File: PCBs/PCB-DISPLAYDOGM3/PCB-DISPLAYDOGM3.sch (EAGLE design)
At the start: 20 parts, among them IC2 74HC14D

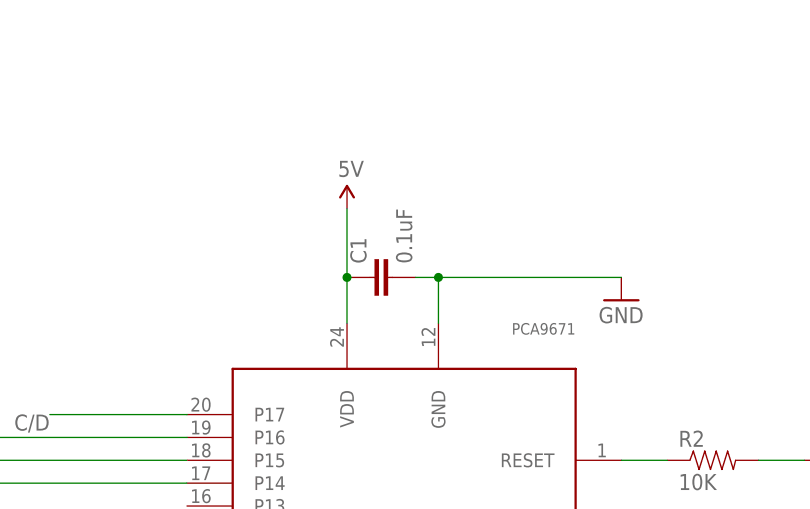
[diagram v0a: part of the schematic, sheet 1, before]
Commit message: Added SKAARHOJ_ID to a lot of PCBs...
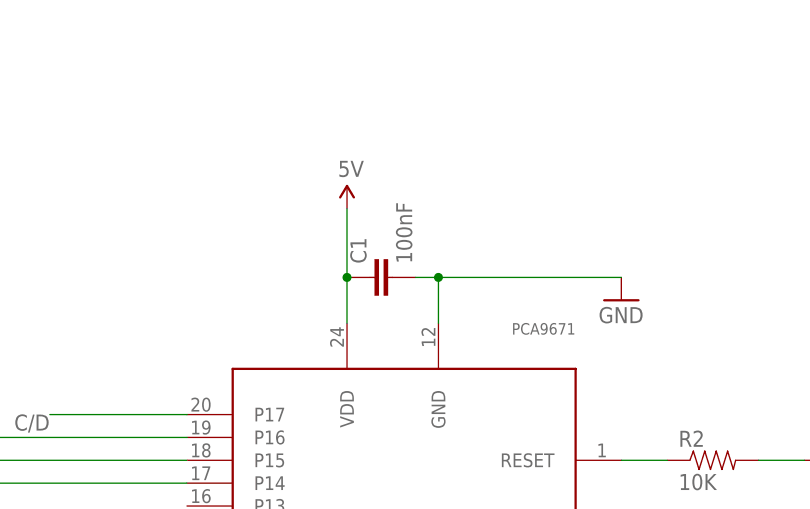
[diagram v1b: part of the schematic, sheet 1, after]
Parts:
- C1: value 0.1uF -> 100nF
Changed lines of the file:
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@@
 <?xml version="1.0" encoding="utf-8"?>
 <!DOCTYPE eagle SYSTEM "eagle.dtd">
-<eagle version="7.5.0">
+<eagle version="7.7.0">
 <drawing>
 <settings>
@@
 <grid distance="0.1" unitdist="inch" unit="inch" style="lines" multiple="1" display="no" altdistance="0.01" altunitdist="inch" altunit="inch"/>
 <layers>
-<layer number="1" name="Top" color="4" fill="1" visible="yes" active="no"/>
-<layer number="2" name="Route2" color="1" fill="3" visible="yes" active="no"/>
-<layer number="3" name="Route3" color="4" fill="3" visible="yes" active="no"/>
-<layer number="4" name="Route4" color="1" fill="4" visible="yes" active="no"/>
-<layer number="5" name="Route5" color="4" fill="4" visible="yes" active="no"/>
-<layer number="6" name="Route6" color="1" fill="8" visible="yes" active="no"/>
-<layer number="7" name="Route7" color="4" fill="8" visible="yes" active="no"/>
-<layer number="8" name="Route8" color="1" fill="2" visible="yes" active="no"/>
-<layer number="9" name="Route9" color="4" fill="2" visible="yes" active="no"/>
-<layer number="10" name="Route10" color="1" fill="7" visible="yes" active="no"/>
-<layer number="11" name="Route11" color="4" fill="7" visible="yes" active="no"/>
-<layer number="12" name="Route12" color="1" fill="5" visible="yes" active="no"/>
-<layer number="13" name="Route13" color="4" fill="5" visible="yes" active="no"/>
-<layer number="14" name="Route14" color="1" fill="6" visible="yes" active="no"/>
-<layer number="15" name="Route15" color="4" fill="6" visible="yes" active="no"/>
-<layer number="16" name="Bottom" color="1" fill="1" visible="yes" active="no"/>
-<layer number="17" name="Pads" color="2" fill="1" visible="yes" active="no"/>
-<layer number="18" name="Vias" color="2" fill="1" visible="yes" active="no"/>
-<layer number="19" name="Unrouted" color="13" fill="1" visible="yes" active="no"/>
-<layer number="20" name="Dimension" color="15" fill="1" visible="yes" active="no"/>
-<layer number="21" name="tPlace" color="7" fill="1" visible="yes" active="no"/>
-<layer number="22" name="bPlace" color="7" fill="1" visible="yes" active="no"/>
-<layer number="23" name="tOrigins" color="15" fill="1" visible="yes" active="no"/>
-<layer number="24" name="bOrigins" color="15" fill="1" visible="yes" active="no"/>
-<layer number="25" name="tNames" color="7" fill="1" visible="yes" active="no"/>
-<layer number="26" name="bNames" color="7" fill="1" visible="yes" active="no"/>
-<layer number="27" name="tValues" color="7" fill="1" visible="yes" active="no"/>
-<layer number="28" name="bValues" color="7" fill="1" visible="yes" active="no"/>
+<layer number="1" name="Top" color="4" fill="1" visible="no" active="no"/>
+<layer number="2" name="Route2" color="1" fill="3" visible="no" active="no"/>
+<layer number="3" name="Route3" color="4" fill="3" visible="no" active="no"/>
+<layer number="4" name="Route4" color="1" fill="4" visible="no" active="no"/>
+<layer number="5" name="Route5" color="4" fill="4" visible="no" active="no"/>
+<layer number="6" name="Route6" color="1" fill="8" visible="no" active="no"/>
+<layer number="7" name="Route7" color="4" fill="8" visible="no" active="no"/>
+<layer number="8" name="Route8" color="1" fill="2" visible="no" active="no"/>
+<layer number="9" name="Route9" color="4" fill="2" visible="no" active="no"/>
+<layer number="10" name="Route10" color="1" fill="7" visible="no" active="no"/>
+<layer number="11" name="Route11" color="4" fill="7" visible="no" active="no"/>
+<layer number="12" name="Route12" color="1" fill="5" visible="no" active="no"/>
+<layer number="13" name="Route13" color="4" fill="5" visible="no" active="no"/>
+<layer number="14" name="Route14" color="1" fill="6" visible="no" active="no"/>
+<layer number="15" name="Route15" color="4" fill="6" visible="no" active="no"/>
+<layer number="16" name="Bottom" color="1" fill="1" visible="no" active="no"/>
+<layer number="17" name="Pads" color="2" fill="1" visible="no" active="no"/>
+<layer number="18" name="Vias" color="2" fill="1" visible="no" active="no"/>
+<layer number="19" name="Unrouted" color="13" fill="1" visible="no" active="no"/>
+<layer number="20" name="Dimension" color="15" fill="1" visible="no" active="no"/>
+<layer number="21" name="tPlace" color="7" fill="1" visible="no" active="no"/>
+<layer number="22" name="bPlace" color="7" fill="1" visible="no" active="no"/>
+<layer number="23" name="tOrigins" color="15" fill="1" visible="no" active="no"/>
+<layer number="24" name="bOrigins" color="15" fill="1" visible="no" active="no"/>
+<layer number="25" name="tNames" color="7" fill="1" visible="no" active="no"/>
+<layer number="26" name="bNames" color="7" fill="1" visible="no" active="no"/>
+<layer number="27" name="tValues" color="7" fill="1" visible="no" active="no"/>
+<layer number="28" name="bValues" color="7" fill="1" visible="no" active="no"/>
 <layer number="29" name="tStop" color="7" fill="3" visible="no" active="no"/>
 <layer number="30" name="bStop" color="7" fill="6" visible="no" active="no"/>
@@
 <layer number="35" name="tGlue" color="7" fill="4" visible="no" active="no"/>
 <layer number="36" name="bGlue" color="7" fill="5" visible="no" active="no"/>
-<layer number="37" name="tTest" color="7" fill="1" visible="yes" active="no"/>
-<layer number="38" name="bTest" color="7" fill="1" visible="yes" active="no"/>
+<layer number="37" name="tTest" color="7" fill="1" visible="no" active="no"/>
+<layer number="38" name="bTest" color="7" fill="1" visible="no" active="no"/>
 <layer number="39" name="tKeepout" color="4" fill="11" visible="no" active="no"/>
 <layer number="40" name="bKeepout" color="1" fill="11" visible="no" active="no"/>
@@
 <layer number="44" name="Drills" color="7" fill="1" visible="no" active="no"/>
 <layer number="45" name="Holes" color="7" fill="1" visible="no" active="no"/>
-<layer number="46" name="Milling" color="3" fill="1" visible="yes" active="no"/>
-<layer number="47" name="Measures" color="7" fill="1" visible="yes" active="no"/>
-<layer number="48" name="Document" color="7" fill="1" visible="yes" active="no"/>
-<layer number="49" name="Reference" color="7" fill="1" visible="yes" active="no"/>
-<layer number="50" name="dxf" color="7" fill="1" visible="yes" active="no"/>
-<layer number="51" name="tDocu" color="7" fill="1" visible="yes" active="no"/>
-<layer number="52" name="bDocu" color="7" fill="1" visible="yes" active="no"/>
-<layer number="53" name="tGND_GNDA" color="7" fill="9" visible="yes" active="no"/>
-<layer number="54" name="bGND_GNDA" color="1" fill="9" visible="yes" active="no"/>
-<layer number="56" name="wert" color="7" fill="1" visible="yes" active="no"/>
-<layer number="57" name="tCAD" color="7" fill="1" visible="yes" active="no"/>
+<layer number="46" name="Milling" color="3" fill="1" visible="no" active="no"/>
+<layer number="47" name="Measures" color="7" fill="1" visible="no" active="no"/>
+<layer number="48" name="Document" color="7" fill="1" visible="no" active="no"/>
+<layer number="49" name="Reference" color="7" fill="1" visible="no" active="no"/>
+<layer number="50" name="dxf" color="7" fill="1" visible="no" active="no"/>
+<layer number="51" name="tDocu" color="7" fill="1" visible="no" active="no"/>
+<layer number="52" name="bDocu" color="7" fill="1" visible="no" active="no"/>
+<layer number="53" name="tGND_GNDA" color="7" fill="9" visible="no" active="no"/>
+<layer number="54" name="bGND_GNDA" color="1" fill="9" visible="no" active="no"/>
+<layer number="56" name="wert" color="7" fill="1" visible="no" active="no"/>
+<layer number="57" name="tCAD" color="7" fill="1" visible="no" active="no"/>
 <layer number="90" name="Modules" color="5" fill="1" visible="yes" active="yes"/>
 <layer number="91" name="Nets" color="2" fill="1" visible="yes" active="yes"/>
@@
 <part name="U$6" library="SparkFun" deviceset="5V" device=""/>
 <part name="GND1" library="SparkFun" deviceset="GND" device=""/>
-<part name="C1" library="SparkFun" deviceset="CAP" device="0603-CAP" value="0.1uF"/>
+<part name="C1" library="SparkFun" deviceset="CAP" device="0603-CAP" value="100nF"/>
 <part name="U$2" library="SKAARHOJ" deviceset="GNDPAD" device="6MM" value="GNDPAD6MM"/>
 <part name="U$20" library="SKAARHOJ" deviceset="GNDPAD" device="6MM" value="GNDPAD6MM"/>

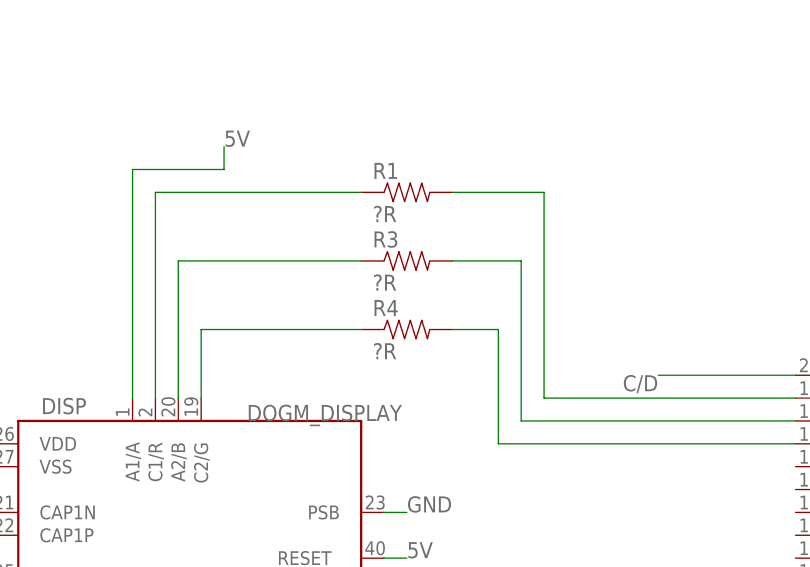
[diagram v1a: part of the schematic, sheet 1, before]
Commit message: New resistor values for the RGB backlight (so balanced for white, less intense)
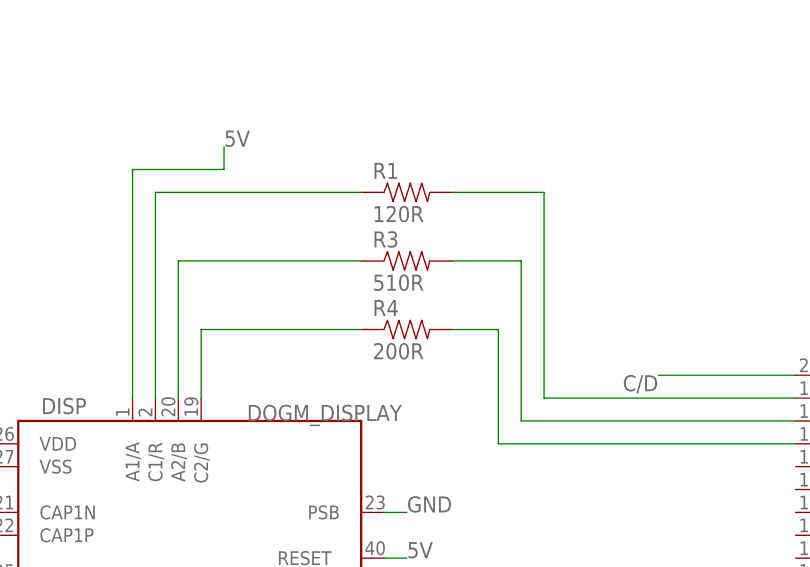
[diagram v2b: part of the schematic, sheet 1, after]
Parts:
- R1: value ?R -> 120R; SKAARHOJ_ID (none) -> SK_120R
- R3: value ?R -> 510R; SKAARHOJ_ID (none) -> SK_510R
- R4: value ?R -> 200R; SKAARHOJ_ID (none) -> SK_200R
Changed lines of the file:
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@@
 <part name="C12" library="SparkFun" deviceset="CAP" device="0603-CAP" value="100nF"/>
 <part name="U$24" library="SparkFun" deviceset="5V" device=""/>
-<part name="R1" library="SparkFun" deviceset="RESISTOR" device="0603-RES" value="?R"/>
-<part name="R3" library="SparkFun" deviceset="RESISTOR" device="0603-RES" value="?R"/>
-<part name="R4" library="SparkFun" deviceset="RESISTOR" device="0603-RES" value="?R"/>
+<part name="R1" library="SparkFun" deviceset="RESISTOR" device="0603-RES" value="120R">
+<attribute name="SKAARHOJ_ID" value="SK_120R"/>
+</part>
+<part name="R3" library="SparkFun" deviceset="RESISTOR" device="0603-RES" value="510R">
+<attribute name="SKAARHOJ_ID" value="SK_510R"/>
+</part>
+<part name="R4" library="SparkFun" deviceset="RESISTOR" device="0603-RES" value="200R">
+<attribute name="SKAARHOJ_ID" value="SK_200R"/>
+</part>
 </parts>
 <sheets>
@@
 <instance part="IC2" gate="C" x="121.92" y="-152.4"/>
 <instance part="IC2" gate="D" x="121.92" y="-170.18"/>
-<instance part="R1" gate="G$1" x="-12.7" y="-12.7"/>
-<instance part="R3" gate="G$1" x="-12.7" y="-20.32"/>
-<instance part="R4" gate="G$1" x="-12.7" y="-27.94"/>
+<instance part="R1" gate="G$1" x="-12.7" y="-12.7">
+<attribute name="SKAARHOJ_ID" x="-12.7" y="-12.7" size="1.778" layer="96" display="off"/>
+</instance>
+<instance part="R3" gate="G$1" x="-12.7" y="-20.32">
+<attribute name="SKAARHOJ_ID" x="-12.7" y="-20.32" size="1.778" layer="96" display="off"/>
+</instance>
+<instance part="R4" gate="G$1" x="-12.7" y="-27.94">
+<attribute name="SKAARHOJ_ID" x="-12.7" y="-27.94" size="1.778" layer="96" display="off"/>
+</instance>
 </instances>
 <busses>

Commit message: d
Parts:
- R1: value 120R -> 120R/1%
- R3: value 510R -> 510R/1%
- R4: value 200R -> 200R/1%
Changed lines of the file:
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@@
 <part name="C12" library="SparkFun" deviceset="CAP" device="0603-CAP" value="100nF"/>
 <part name="U$24" library="SparkFun" deviceset="5V" device=""/>
-<part name="R1" library="SparkFun" deviceset="RESISTOR" device="0603-RES" value="120R">
+<part name="R1" library="SparkFun" deviceset="RESISTOR" device="0603-RES" value="120R/1%">
 <attribute name="SKAARHOJ_ID" value="SK_120R"/>
 </part>
-<part name="R3" library="SparkFun" deviceset="RESISTOR" device="0603-RES" value="510R">
+<part name="R3" library="SparkFun" deviceset="RESISTOR" device="0603-RES" value="510R/1%">
 <attribute name="SKAARHOJ_ID" value="SK_510R"/>
 </part>
-<part name="R4" library="SparkFun" deviceset="RESISTOR" device="0603-RES" value="200R">
+<part name="R4" library="SparkFun" deviceset="RESISTOR" device="0603-RES" value="200R/1%">
 <attribute name="SKAARHOJ_ID" value="SK_200R"/>
 </part>
